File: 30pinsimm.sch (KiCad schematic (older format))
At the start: 7 parts, among them U1 JEDEC-FPDRAM_xMbx4, U2 JEDEC-FPDRAM_xMbx4, U3 JEDEC-FPDRAM_xMbx1

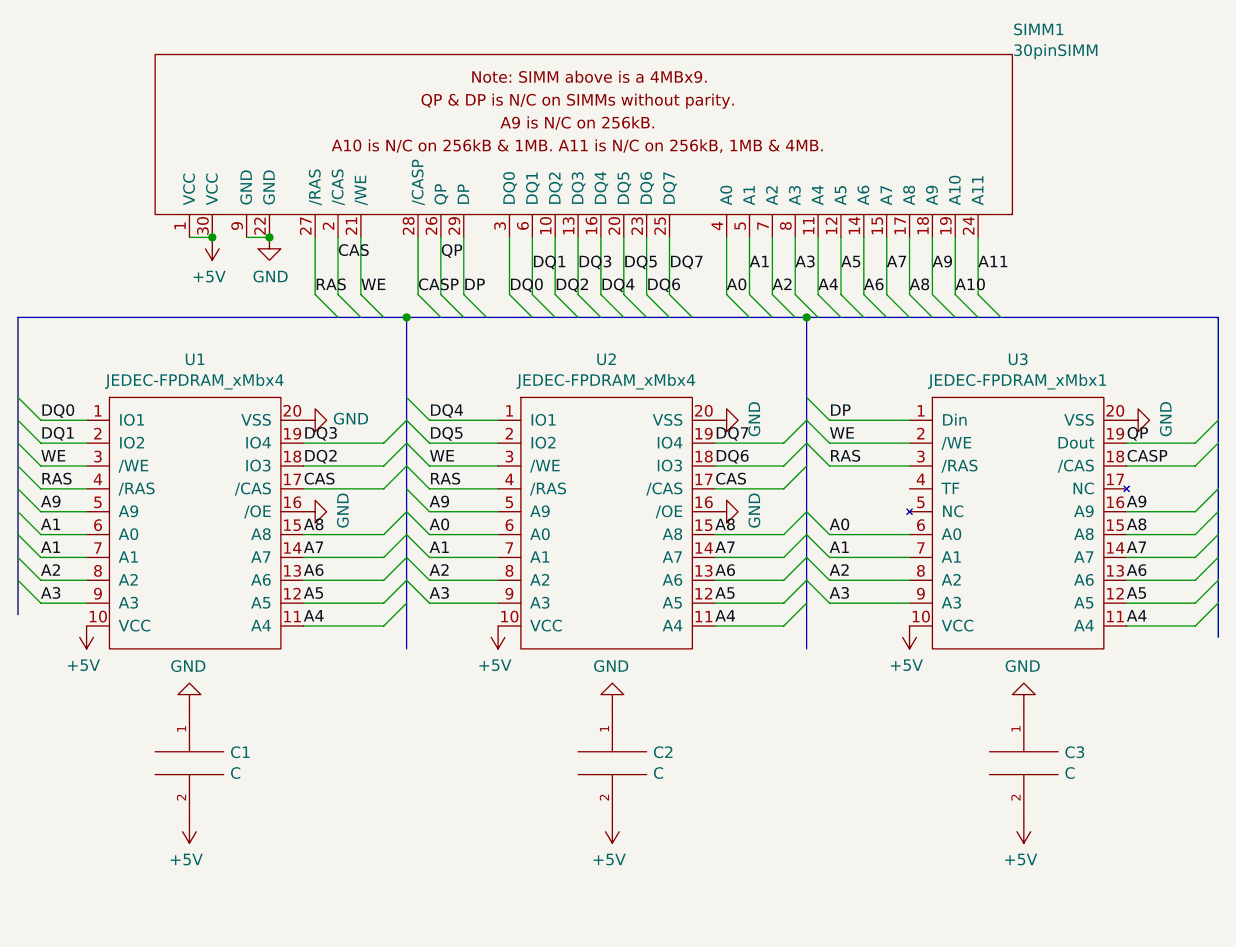
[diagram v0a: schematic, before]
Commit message: updated the 4Mb module
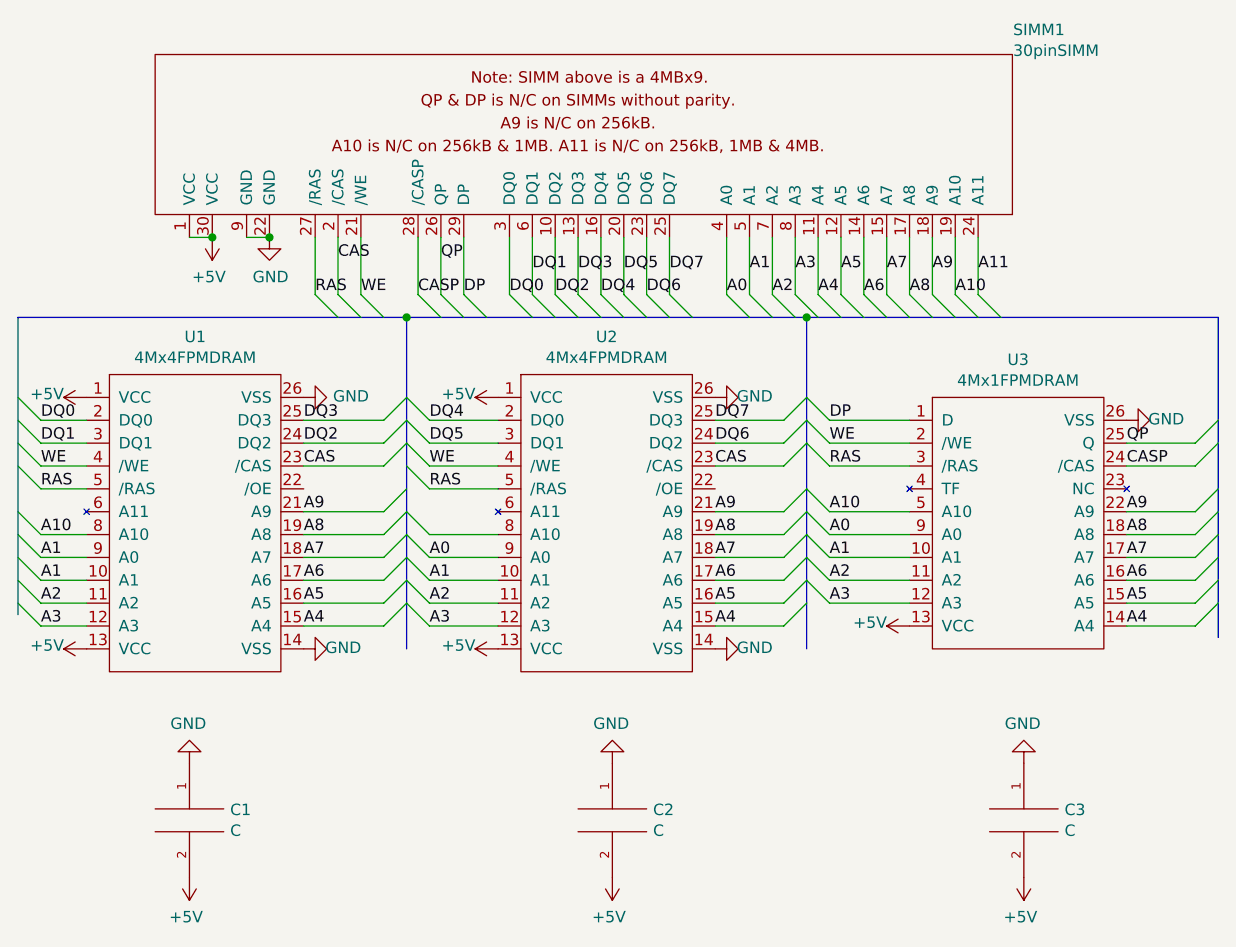
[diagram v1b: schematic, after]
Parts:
- removed U1, U2: JEDEC-FPDRAM_xMbx4, Sebs:SOJ-20-26-2, symbol Sebs:JEDEC-FPDRAM_xMbx4
- removed U3: JEDEC-FPDRAM_xMbx1, Sebs:SOJ-20-26-2, symbol Sebs:JEDEC-FPDRAM_xMbx1
- added U1, U2: 4Mx4FPMDRAM, Sebs:SOJ-24, symbol Sebs:4Mx4FPMDRAM
- added U3: 4Mx1FPMDRAM, Sebs:SOJ-20, symbol Sebs:4Mx1FPMDRAM
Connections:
- net +5V: now also U1.1 (VCC), U1.13 (VCC), U2.1 (VCC), U2.13 (VCC), U3.13 (VCC)
- net A0: now also U2.9 (A0), U3.9 (A0)
- net A1: now also U1.10 (A1), U1.9 (A0), U2.10 (A1), U3.10 (A1)
- net A10: now also U1.8 (A10), U3.5 (A10)
- net A2: now also U1.11 (A2), U2.11 (A2), U3.11 (A2)
- net A3: now also U1.12 (A3), U2.12 (A3), U3.12 (A3)
- net A4: now also U1.15 (A4), U2.15 (A4), U3.14 (A4)
- net A5: now also U1.16 (A5), U2.16 (A5), U3.15 (A5)
- net A6: now also U1.17 (A6), U2.17 (A6), U3.16 (A6)
- net A7: now also U1.18 (A7), U2.18 (A7), U3.17 (A7)
- net A8: now also U1.19 (A8), U2.19 (A8), U3.18 (A8)
- net A9: now also U1.21 (A9), U2.21 (A9), U3.22 (A9)
- net CAS: now also U1.23 (/CAS), U2.23 (/CAS)
- net CASP: now also U3.24 (/CAS)
- net DP: now also U3.1 (D)
- net DQ0: now also U1.2 (DQ0)
- net DQ1: now also U1.3 (DQ1)
- net DQ2: now also U1.24 (DQ2)
- net DQ3: now also U1.25 (DQ3)
- net DQ4: now also U2.2 (DQ0)
- net DQ5: now also U2.3 (DQ1)
- net DQ6: now also U2.24 (DQ2)
- net DQ7: now also U2.25 (DQ3)
- net GND: now also U1.14 (VSS), U1.26 (VSS), U2.14 (VSS), U2.26 (VSS), U3.26 (VSS)
- net QP: now also U3.25 (Q)
- net RAS: now also U1.5 (/RAS), U2.5 (/RAS), U3.3 (/RAS)
- net WE: now also U1.4 (/WE), U2.4 (/WE), U3.2 (/WE)
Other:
- moved on the sheet: C1, C2, C3

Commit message: general updates
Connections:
- net A10: now also U2.8 (A10)
- net GND: now also U1.22 (/OE), U2.22 (/OE)
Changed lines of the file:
@@
 Text Label 6700 4100 0    50   ~ 0
 A10
-Wire Bus Line
-	3150 3250 4850 3250
-Wire Bus Line
-	8400 3250 8400 4650
-Wire Bus Line
-	6600 3250 6600 4700
-Wire Bus Line
-	6600 3250 8400 3250
-Wire Bus Line
-	4850 3250 4850 4700
-Wire Bus Line
-	3150 3250 3150 4550
-Wire Bus Line
-	4850 3250 6600 3250
 $Comp
 L Sebs:4Mx4FPMDRAM U1
@@
 	1    0    0    -1
 $EndComp
+Text Label 4950 4200 0    50   ~ 0
+A10
+Wire Bus Line
+	3150 3250 4850 3250
+Wire Bus Line
+	8400 3250 8400 4650
+Wire Bus Line
+	6600 3250 6600 4700
+Wire Bus Line
+	6600 3250 8400 3250
+Wire Bus Line
+	4850 3250 4850 4700
+Wire Bus Line
+	3150 3250 3150 4550
+Wire Bus Line
+	4850 3250 6600 3250
+$Comp
+L power:GND #PWR?
+U 1 1 5FF5D9AB
+P 4400 4000
+F 0 "#PWR?" H 4400 3750 50  0001 C CNN
+F 1 "GND" V 4405 3827 50  0000 C CNN
+F 2 "" H 4400 4000 50  0001 C CNN
+F 3 "" H 4400 4000 50  0001 C CNN
+	1    4400 4000
+	0    -1   -1   0
+$EndComp
+$Comp
+L power:GND #PWR?
+U 1 1 5FF5E134
+P 6200 4000
+F 0 "#PWR?" H 6200 3750 50  0001 C CNN
+F 1 "GND" V 6205 3827 50  0000 C CNN
+F 2 "" H 6200 4000 50  0001 C CNN
+F 3 "" H 6200 4000 50  0001 C CNN
+	1    6200 4000
+	0    -1   -1   0
+$EndComp
 $EndSCHEMATC

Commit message: 2sig 2 pwr layer routing
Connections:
- net A0: now also U1.9 (A0)
- net A1: no longer U1.9 (A0)
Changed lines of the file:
@@
 encoding utf-8
 Sheet 1 1
-Title ""
-Date ""
-Rev ""
-Comp ""
-Comment1 ""
+Title "4Mbyte 30 Pin SIMM 8/9 Bit FPM DRAM Module"
+Date "2021-01-02"
+Rev "v0.2"
+Comp "https://pcb.hegars.com/?sku=4mbfpmsimm"
+Comment1 "https://github.com/hegars/30pinSIMM/"
 Comment2 ""
 Comment3 ""
@@
 A9
 Text Label 3250 4300 0    50   ~ 0
-A1
+A0
 Text Label 3250 4400 0    50   ~ 0
 A1
@@
 Text Label 4950 4600 0    50   ~ 0
 A3
-Text Label 6250 3150 0    50   ~ 0
+Text Label 6250 3150 1    50   ~ 0
 A0
-Text Label 6350 3050 0    50   ~ 0
+Text Label 6350 3150 1    50   ~ 0
 A1
-Text Label 6450 3150 0    50   ~ 0
+Text Label 6450 3150 1    50   ~ 0
 A2
-Text Label 6550 3050 0    50   ~ 0
+Text Label 6550 3150 1    50   ~ 0
 A3
-Text Label 6650 3150 0    50   ~ 0
+Text Label 6650 3150 1    50   ~ 0
 A4
-Text Label 6750 3050 0    50   ~ 0
+Text Label 6750 3150 1    50   ~ 0
 A5
-Text Label 6850 3150 0    50   ~ 0
+Text Label 6850 3150 1    50   ~ 0
 A6
-Text Label 6950 3050 0    50   ~ 0
+Text Label 6950 3150 1    50   ~ 0
 A7
-Text Label 7050 3150 0    50   ~ 0
+Text Label 7050 3150 1    50   ~ 0
 A8
-Text Label 7150 3050 0    50   ~ 0
+Text Label 7150 3150 1    50   ~ 0
 A9
-Text Label 7250 3150 0    50   ~ 0
+Text Label 7250 3150 1    50   ~ 0
 A10
-Text Label 7350 3050 0    50   ~ 0
+Text Label 7350 3150 1    50   ~ 0
 A11
-Text Label 5300 3150 0    50   ~ 0
+Text Label 5300 3150 1    50   ~ 0
 DQ0
-Text Label 5400 3050 0    50   ~ 0
+Text Label 5400 3150 1    50   ~ 0
 DQ1
-Text Label 5500 3150 0    50   ~ 0
+Text Label 5500 3150 1    50   ~ 0
 DQ2
-Text Label 5600 3050 0    50   ~ 0
+Text Label 5600 3150 1    50   ~ 0
 DQ3
-Text Label 5700 3150 0    50   ~ 0
+Text Label 5700 3150 1    50   ~ 0
 DQ4
-Text Label 5800 3050 0    50   ~ 0
+Text Label 5800 3150 1    50   ~ 0
 DQ5
-Text Label 5900 3150 0    50   ~ 0
+Text Label 5900 3150 1    50   ~ 0
 DQ6
-Text Label 6000 3050 0    50   ~ 0
+Text Label 6000 3150 1    50   ~ 0
 DQ7
-Text Label 4900 3150 0    50   ~ 0
+Text Label 4900 3150 1    50   ~ 0
 CASP
-Text Label 5000 3000 0    50   ~ 0
+Text Label 5000 3150 1    50   ~ 0
 QP
-Text Label 5100 3150 0    50   ~ 0
+Text Label 5100 3150 1    50   ~ 0
 DP
-Text Label 4450 3150 0    50   ~ 0
+Text Label 4450 3150 1    50   ~ 0
 RAS
-Text Label 4550 3000 0    50   ~ 0
+Text Label 4550 3150 1    50   ~ 0
 CAS
 Text Label 4400 4600 0    50   ~ 0
@@
 Wire Wire Line
 	4650 2900 4650 3150
-Text Label 4650 3150 0    50   ~ 0
+Text Label 4650 3150 1    50   ~ 0
 WE
 Entry Wire Line
@@
 	4850 3250 6600 3250
 $Comp
-L power:GND #PWR?
+L power:GND #PWR0111
 U 1 1 5FF5D9AB
 P 4400 4000
-F 0 "#PWR?" H 4400 3750 50  0001 C CNN
+F 0 "#PWR0111" H 4400 3750 50  0001 C CNN
 F 1 "GND" V 4405 3827 50  0000 C CNN
 F 2 "" H 4400 4000 50  0001 C CNN
@@
 $EndComp
 $Comp
-L power:GND #PWR?
+L power:GND #PWR0112
 U 1 1 5FF5E134
 P 6200 4000
-F 0 "#PWR?" H 6200 3750 50  0001 C CNN
+F 0 "#PWR0112" H 6200 3750 50  0001 C CNN
 F 1 "GND" V 6205 3827 50  0000 C CNN
 F 2 "" H 6200 4000 50  0001 C CNN
